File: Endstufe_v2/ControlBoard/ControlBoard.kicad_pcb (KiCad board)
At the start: 4 copper layers, 100 x 85 mm, 231 parts, among them J1 B4B-XH-2_(LF)(SN), J10 DNP, J11 DNP, J12 DNP, J13 DNP, J14 DAC all outputs, J15 B4B-XH-2_(LF)(SN), J16 B6B-XH-2(LF)(SN), J17 Conn_01x02_Pin, J18 Conn_01x02_Pin, J19 Conn_01x06_Pin, J2 B4B-XH-2_(LF)(SN), J3 B4B-XH-2_(LF)(SN), J4 DNP, J5 B6B-XH-2(LF)(SN), J6 Conn_01x02_Pin, J7 DNP, J8 DNP, J9 DNP, SW1 TS-1187A-B-A-B, SW2 TS-1187A-B-A-B, U1 NVTFWS014P04M8LTAG, U10 ADAU1962AWBSTZ, U2 1SMA5927A, U3 TPS62933, U4 TYPE-C 16PFS 2JCB1.2-H6.5 IPX8, U5 W25Q128JVS, U6 RP2040, U7 W25Q128JVS, U8 ADAU1467WBCPZ300, U9 ZPLR135_T8, Y1 12Mhz, Y2 24.576Mhz, Y3 24.576Mhz

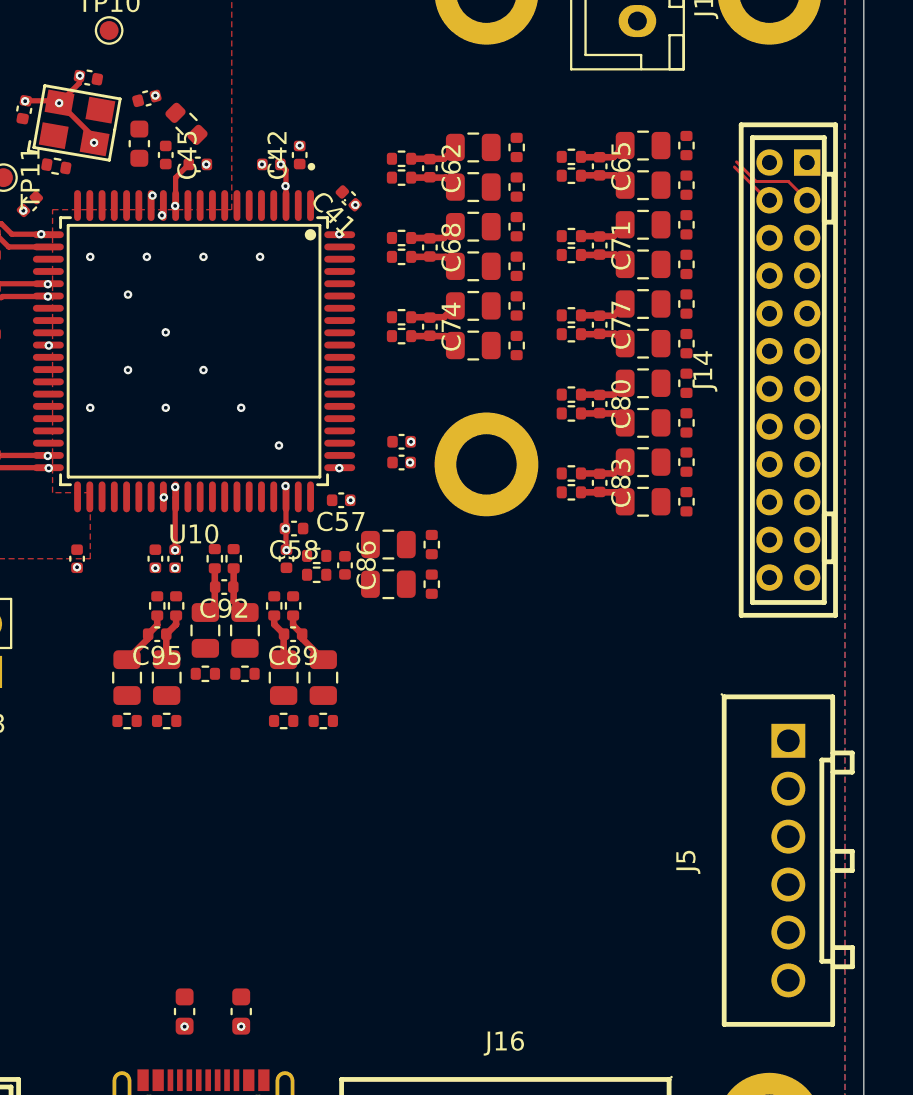
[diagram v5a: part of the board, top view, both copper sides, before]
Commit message: Routed DAC outputs
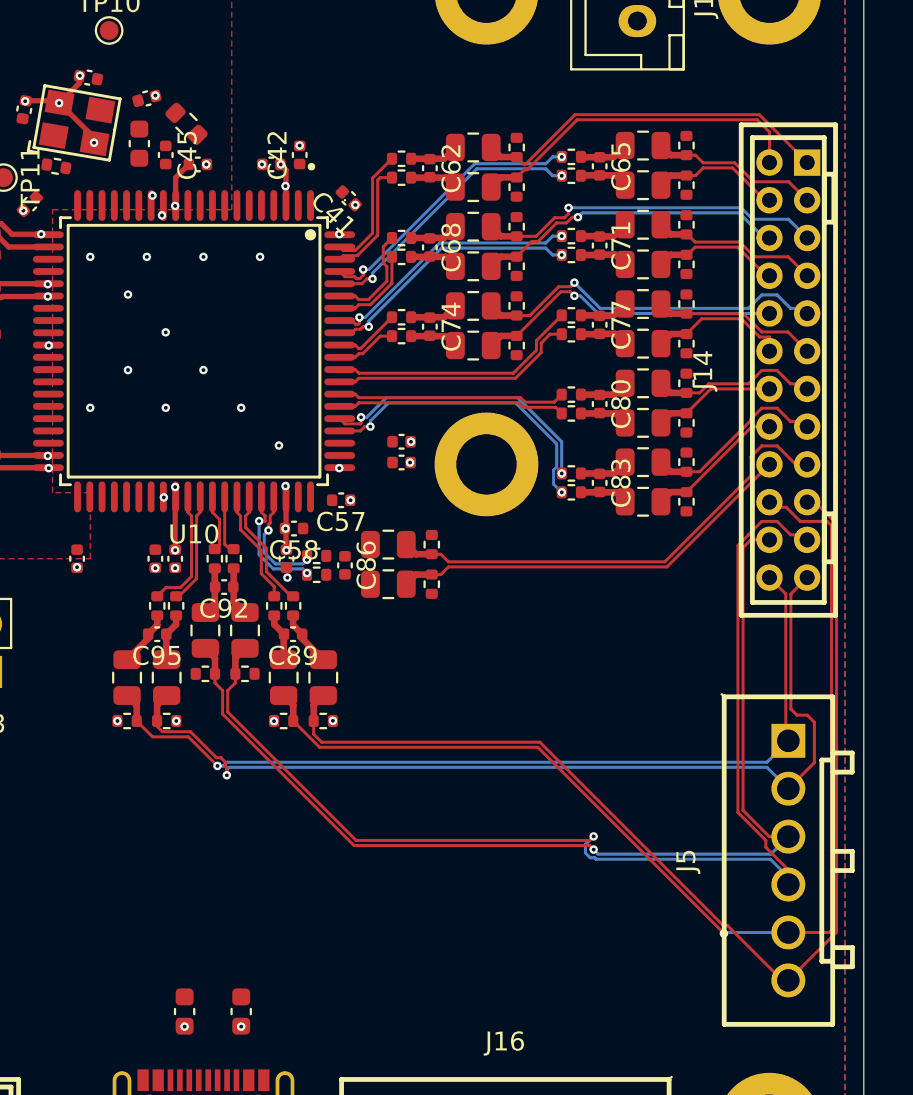
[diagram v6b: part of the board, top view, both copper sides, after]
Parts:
- turned R28 to -90 degrees
- turned R29 to 90 degrees
- turned R32 to -90 degrees
- turned R33 to 90 degrees
- turned R36 to -90 degrees
- turned R37 to 90 degrees
- turned R40 to -90 degrees
- turned R41 to 90 degrees
- turned R44 to -90 degrees
- turned R45 to 90 degrees
- turned R48 to -90 degrees
- turned R49 to 90 degrees
- turned R52 to -90 degrees
- turned R53 to 90 degrees
- turned R60 to -90 degrees
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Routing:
- net /ADAU1962A/DAC2N: track 0.00 -> 62.5 mm, vias 0 -> 1
- net /ADAU1962A/DAC3N: track 0.00 -> 60.5 mm
- net /ADAU1962A/DAC3P: track 0.00 -> 60.1 mm, vias 0 -> 1
- net /ADAU1962A/DAC2P: track 0.00 -> 55.8 mm, vias 0 -> 1
- net /ADAU1962A/DAC1N: track 0.00 -> 50.5 mm, vias 0 -> 1
- net /ADAU1962A/DAC1P: track 0.00 -> 46.7 mm, vias 0 -> 1
- net /ADAU1962A/DAC_Filter8/OUTPUTxN: track 0.00 -> 25.2 mm
- net /ADAU1962A/DAC_Filter8/OUTPUTxP: track 0.00 -> 21.9 mm
- net /ADAU1962A/DAC_Filter/OUTPUTxN: track 0.00 -> 19.3 mm
- net /ADAU1962A/DAC_Filter4/OUTPUTxN: track 0.00 -> 18.9 mm, vias 0 -> 1
- net /ADAU1962A/DAC_Filter2/OUTPUTxN: track 0.00 -> 18.4 mm, vias 0 -> 1
- net /ADAU1962A/DAC_Filter/OUTPUTxP: track 0.00 -> 18.1 mm
- net /ADAU1962A/DAC_Filter2/OUTPUTxP: track 0.00 -> 16.5 mm, vias 0 -> 1
- net /ADAU1962A/DAC_Filter4/OUTPUTxP: track 0.00 -> 16.4 mm, vias 0 -> 1
- net /ADAU1962A/DAC_Filter7/DACxP: track 0.00 -> 16.0 mm, vias 0 -> 2
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
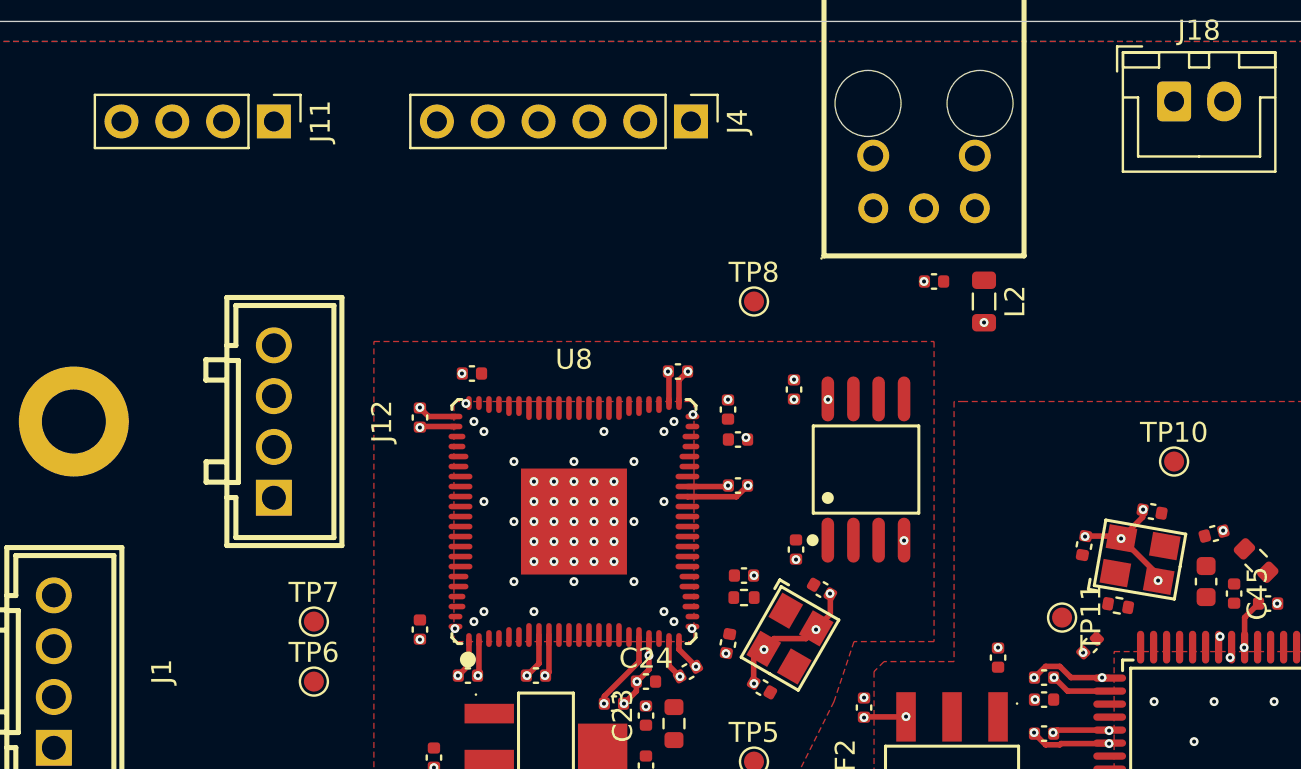
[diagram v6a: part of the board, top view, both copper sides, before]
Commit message: Route control board (continued)
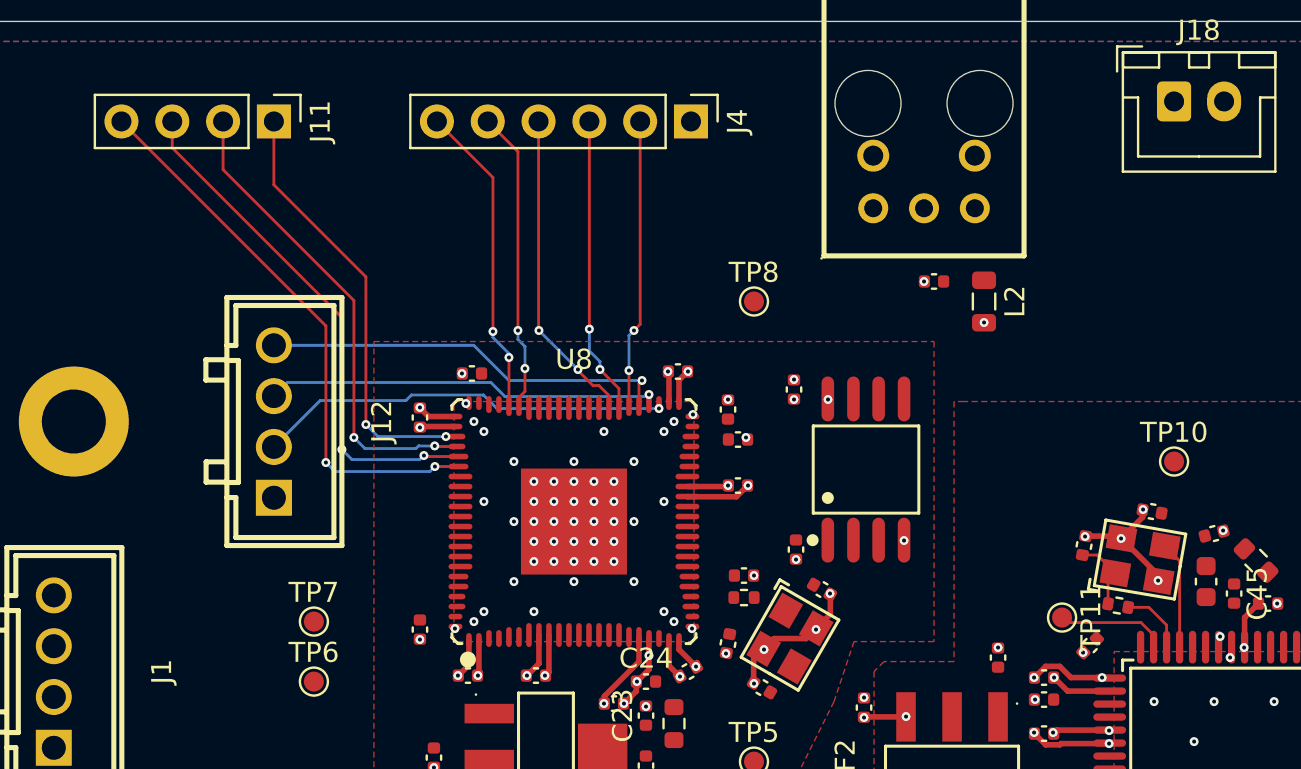
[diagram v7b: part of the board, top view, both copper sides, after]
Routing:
- net Net-(J11-Pin_4): track 0.00 -> 28.2 mm, vias 0 -> 2
- net Net-(J11-Pin_3): track 0.00 -> 26.1 mm, vias 0 -> 2
- net Net-(J11-Pin_2): track 0.00 -> 24.0 mm, vias 0 -> 2
- net Net-(J11-Pin_1): track 0.00 -> 21.9 mm, vias 0 -> 2
- net Net-(J12-Pin_2): track 0.00 -> 20.8 mm, vias 0 -> 1
- net Net-(J12-Pin_4): track 0.00 -> 20.5 mm, vias 0 -> 1
- net Net-(J12-Pin_3): track 0.00 -> 19.9 mm, vias 0 -> 1
- net /ADAU1467/DAC_DATA0: track 0.00 -> 16.0 mm, vias 0 -> 2
- net /ADAU1467/DAC_DATA2: track 0.00 -> 15.7 mm, vias 0 -> 2
- net /ADAU1467/DAC_DATA1: track 0.00 -> 15.1 mm, vias 0 -> 2
- net /ADAU1467/DAC_BLCK: track 0.00 -> 14.9 mm, vias 0 -> 2
- net /ADAU1467/DAC_LRCLK: track 0.00 -> 14.5 mm, vias 0 -> 2
- net Net-(U10-MCLKO): track 0.00 -> 5.54 mm
- net /ADAU1962A/XTALI: track 0.00 -> 5.36 mm
- net Net-(C44-Pad1): track 0.00 -> 3.71 mm
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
